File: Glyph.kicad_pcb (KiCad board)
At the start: 2 copper layers, 98 x 40.5 mm, 32 parts, among them J0 Battery Pads, J1 Shard, J2 USB-Micro, SW0 RESET, SW1 UP, SW2 DOWN, SW3 LEFT, SW4 RIGHT, SW5 BTN_A, SW6 BTN_B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

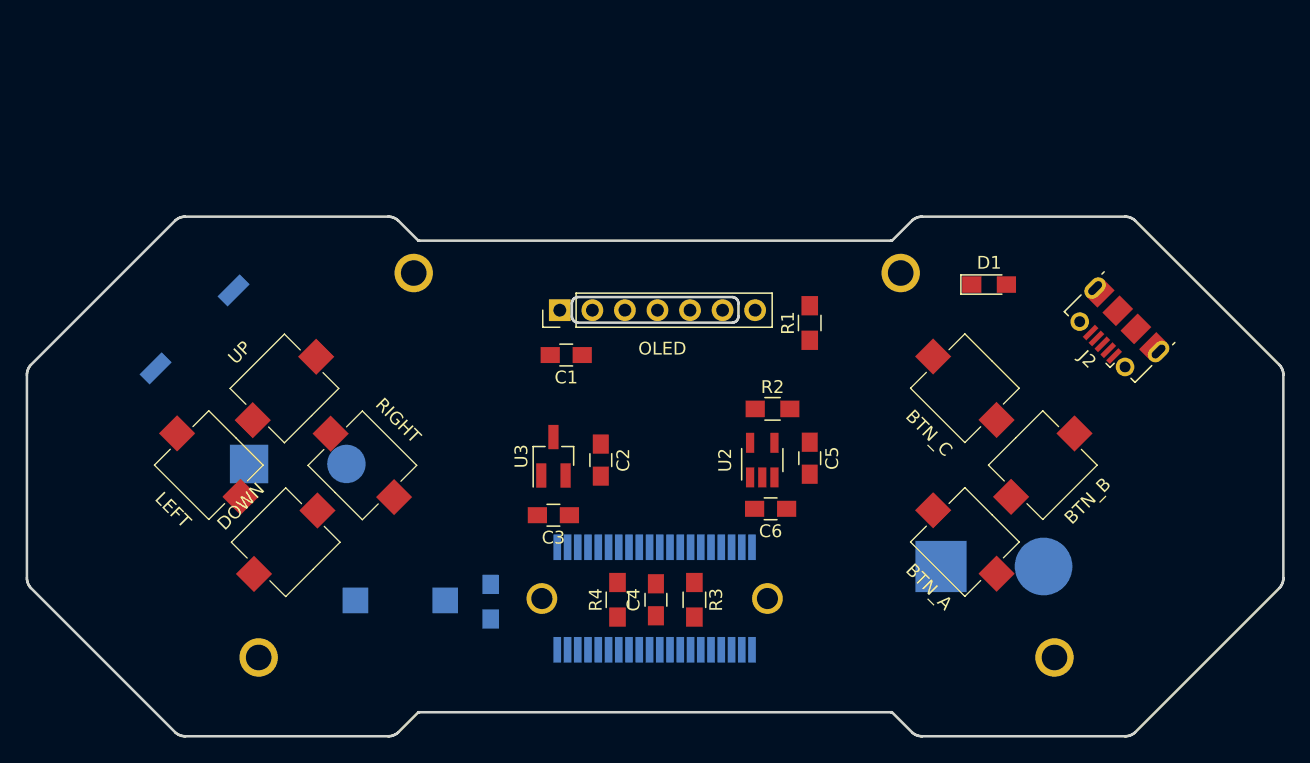
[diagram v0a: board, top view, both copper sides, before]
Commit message: initial oled components
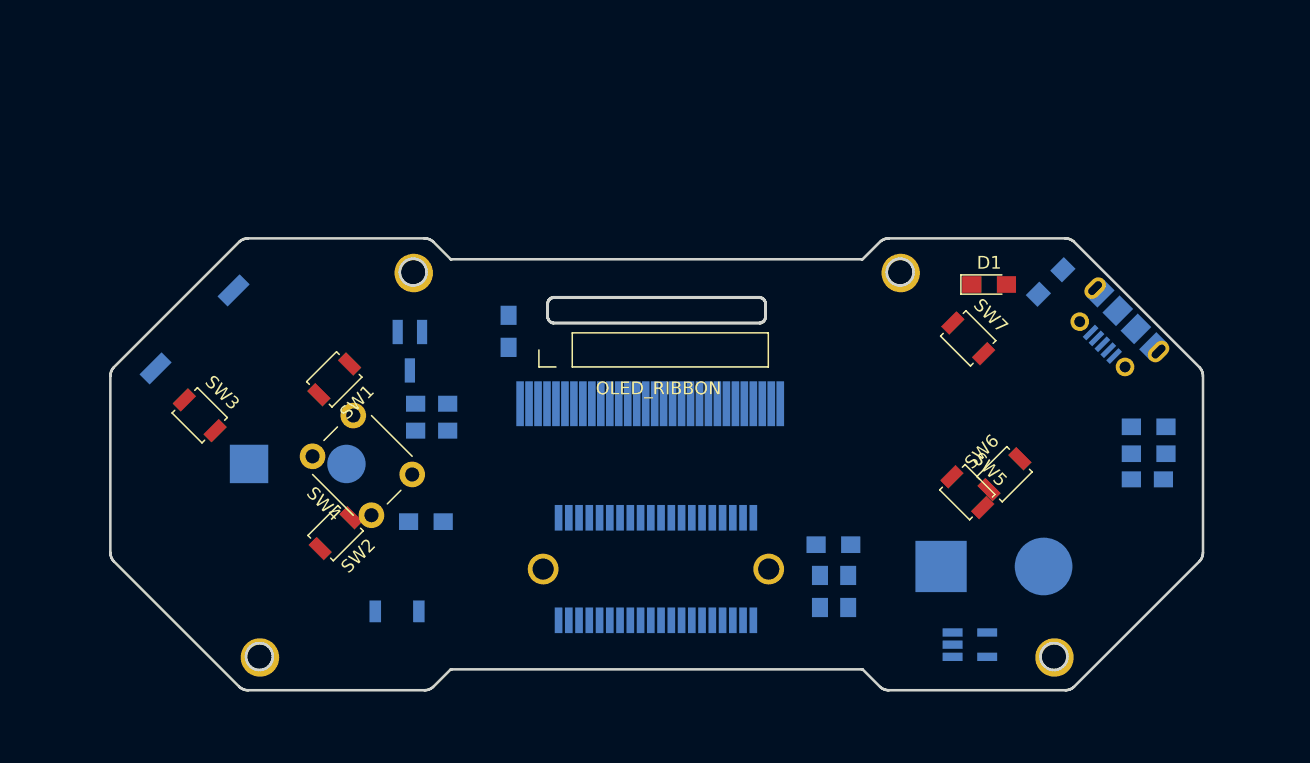
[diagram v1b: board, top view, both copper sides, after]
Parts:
- removed U1: OLED, Custom Footprints:128x64-OLED
- removed X1, X2, X3, X4: hole, Custom Footprints:M2_SCREW_HOLE
- added J3: Screw Point 1, Custom Footprints:M2_SCREW_HOLE, F.Cu at (187.1, 118.1)
- added J4: Screw Point 2, Custom Footprints:M2_SCREW_HOLE, F.Cu at (125.1, 118.1)
- added J5: Screw Point 3, Custom Footprints:M2_SCREW_HOLE, F.Cu at (137.1, 88.1)
- added J6: Screw Point 4, Custom Footprints:M2_SCREW_HOLE, F.Cu at (175.1, 88.1)
- added J7: OLED_RIBBON, Custom Footprints:1.3-OLED-bare, F.Cu at (148.2, 94.1)
- C1, C2, C3, C4, C5, C6, J2, R1, R2, R3, R4, U2, U3: moved to B.Cu
- SW0, SW1, SW2, SW3, SW5, SW6, SW7: footprint Custom Footprints:SW_SOFT_SMD_6mm -> Buttons_Switches_SMD:SW_SPST_B3U-1000P
- SW4: footprint Custom Footprints:SW_SOFT_SMD_6mm -> Buttons_Switches_THT:SW_PUSH_6mm
- moved R4 43.0 mm to (194.4, 102.2), turned to 0 degrees
- moved C4 39.5 mm to (194.3, 104.2), turned to 0 degrees
- moved R3 37.9 mm to (194.4, 100.1), turned to 180 degrees
- moved U2 21.7 mm to (180.5, 117.1), turned to 0 degrees
- moved R1 19.1 mm to (186.8, 88.8), turned to 45 degrees
- moved U3 13.9 mm to (136.8, 94.2), turned to 270 degrees
- moved C2 13.4 mm to (138.5, 100.4), turned to 180 degrees
- moved C3 12.9 mm to (138.5, 98.3)
- moved R2 11.6 mm to (169.8, 109.3)
- moved C5 10.8 mm to (171.0, 113.0), turned to 90 degrees
- moved R0 8.04 mm to (138.1, 107.5), turned to 180 degrees
- moved C6 7.51 mm to (168.8, 113.0), turned to 270 degrees
- moved C1 4.87 mm to (144.5, 92.7), turned to 270 degrees
- moved SW0 3.31 mm to (135.8, 114.5)
- moved J1 2.30 mm to (163.6, 111.2)
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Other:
- board size 98 x 40.5 mm -> 85.3 x 35.3 mm

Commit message: added OLED circuit
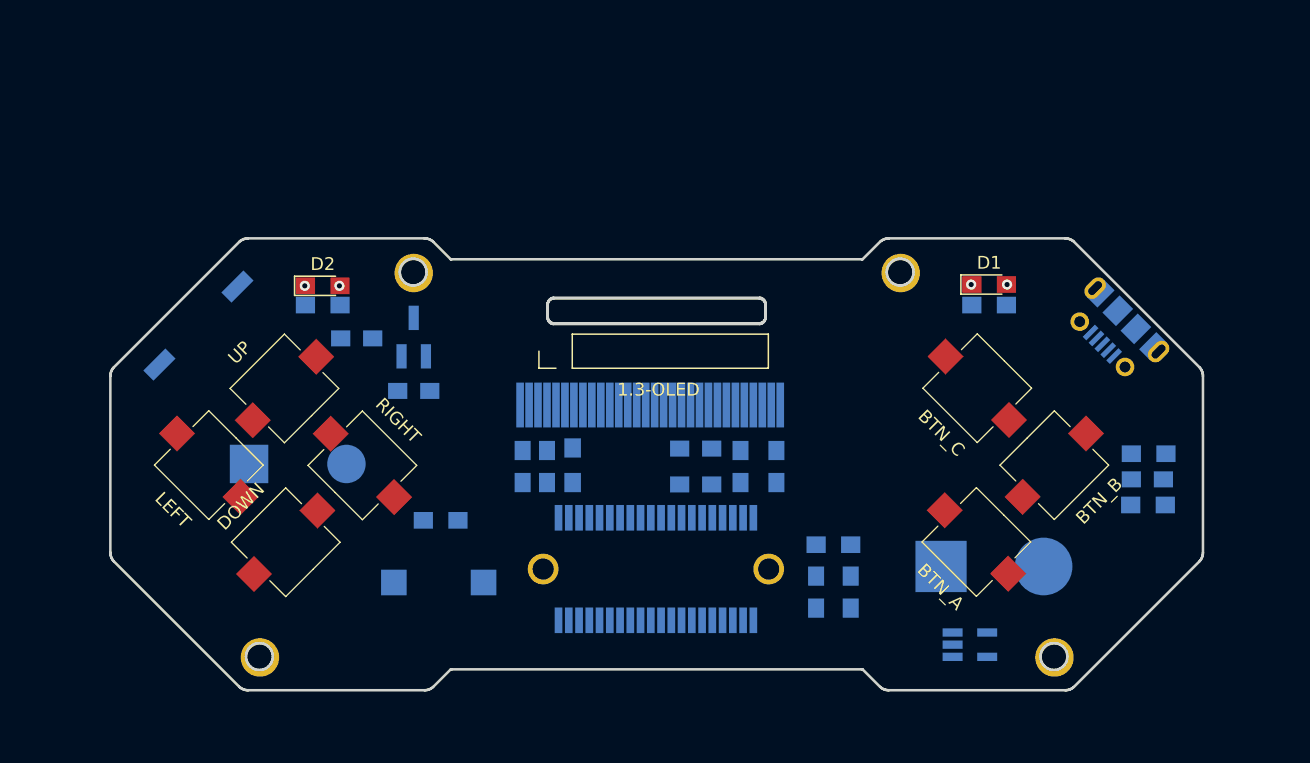
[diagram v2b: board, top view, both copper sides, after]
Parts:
- removed C1: 104, Capacitors_SMD:C_0805_HandSoldering
- removed J7: OLED_RIBBON, Custom Footprints:1.3-OLED-bare
- added C10: 1uF, Capacitors_SMD:C_0805_HandSoldering, B.Cu at (162.6, 103.2)
- added C11: 1uF, Capacitors_SMD:C_0805_HandSoldering, B.Cu at (165.4, 103.2)
- added C12: 104, Capacitors_SMD:C_0805_HandSoldering, B.Cu at (159.1, 101.8)
- added C7: 104, Capacitors_SMD:C_0805_HandSoldering, B.Cu at (159.1, 104.6)
- added C8: 47uF, Capacitors_SMD:C_0805_HandSoldering, B.Cu at (145.6, 103.2)
- added C9: 22uF, Capacitors_SMD:C_0805_HandSoldering, B.Cu at (147.5, 103.2)
- added D2: USR, LEDs:LED_0805_HandSoldering, F.Cu at (130.0, 89.1)
- added R5: 390k, Resistors_SMD:R_0805_HandSoldering, B.Cu at (149.5, 103.1)
- added R6: LED, Resistors_SMD:R_0805_HandSoldering, B.Cu at (130.0, 90.6)
- added U1: 1.3-OLED, Custom Footprints:1.3-OLED-bare, F.Cu at (148.2, 94.2)
- SW0, SW1, SW2, SW3, SW5, SW6, SW7: footprint Buttons_Switches_SMD:SW_SPST_B3U-1000P -> Custom Footprints:SW_SOFT_SMD_6mm
- SW4: footprint Buttons_Switches_THT:SW_PUSH_6mm -> Custom Footprints:SW_SOFT_SMD_6mm
- moved C2 9.28 mm to (132.7, 93.2)
- moved R3 6.10 mm to (194.4, 106.2)
- moved R1 5.13 mm to (182.0, 90.6), turned to 0 degrees
- moved C5 2.50 mm to (168.5, 113.0)
- moved C6 2.40 mm to (171.2, 113.0)
- moved C3 1.72 mm to (137.1, 97.3), turned to 0 degrees
- moved R0 1.15 mm to (139.2, 107.4)
- moved U3 1.14 mm to (137.1, 93.1), turned to 90 degrees
- moved SW8 0.42 mm to (120.3, 92.2), turned to 225 degrees
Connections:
- J1 pad 18: (no net) -> USR_LED
- J1 pad 22: D_DC -> D_RST
- J1 pad 24: D_RST -> D_DC
- J1 pad 26: D_MOSI -> D_SCK
- J1 pad 28: D_SCK -> D_MOSI
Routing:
- net USR_LED: vias 0 -> 1
- net Net-(D2-Pad1): vias 0 -> 1
- net Net-(D1-Pad1): vias 0 -> 1
- net CHARGE: vias 0 -> 1

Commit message: update layout
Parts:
- moved C8 4.24 mm to (147.0, 99.2)
- moved C9 4.18 mm to (148.7, 99.2)
- moved U3 4.12 mm to (138.1, 97.1), turned to 45 degrees
- moved R5 4.10 mm to (150.4, 99.1)
- moved C11 4.03 mm to (164.9, 99.2)
- moved C7 4.00 mm to (159.3, 100.6)
- moved C10 4.00 mm to (162.5, 99.2)
- moved C3 3.91 mm to (140.4, 99.4), turned to 45 degrees
- moved C2 3.53 mm to (135.8, 94.8), turned to 45 degrees
- moved C12 3.31 mm to (159.3, 98.5)
- moved R1 1.60 mm to (182.1, 89.0)
- moved R6 1.50 mm to (130.1, 89.1)
- moved C5 1.22 mm to (169.2, 112.0)
- moved R4 1.10 mm to (194.5, 103.3)
- moved C6 1.02 mm to (171.0, 112.0)
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
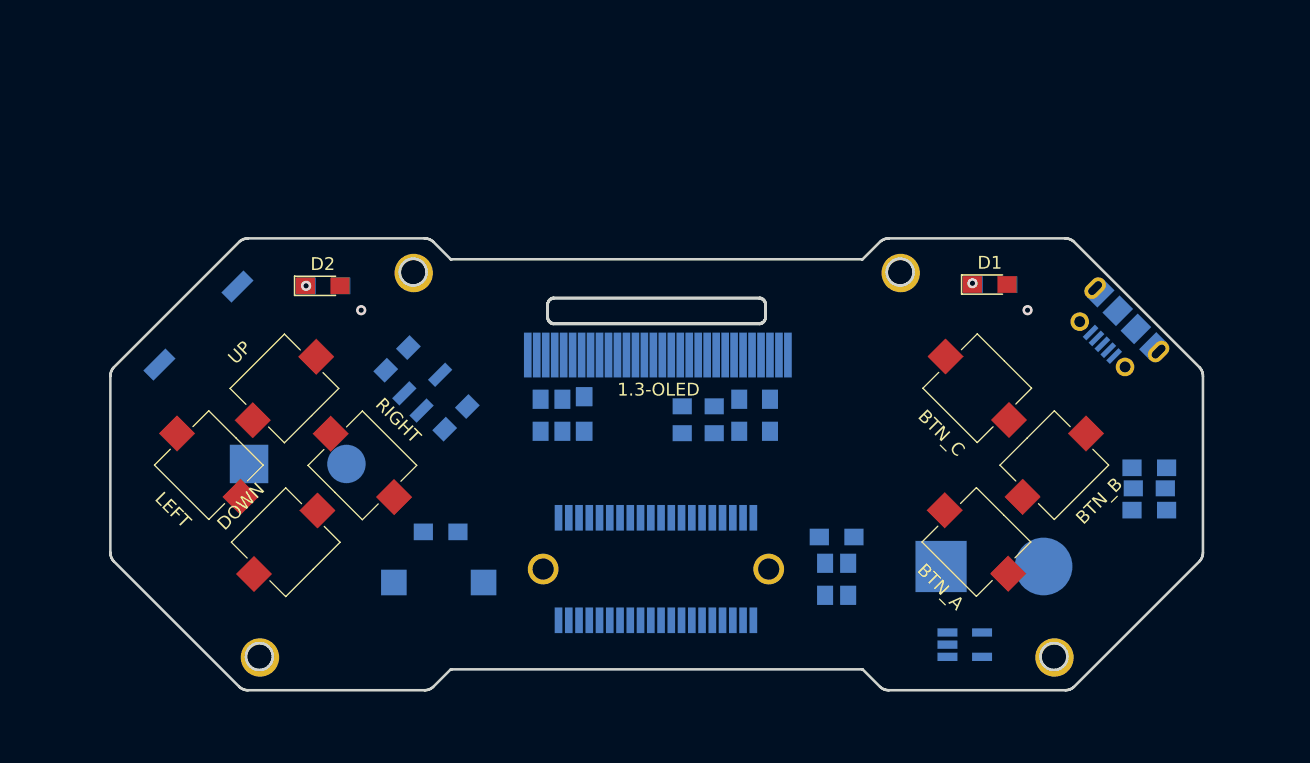
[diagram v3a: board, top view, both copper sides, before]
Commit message: new layout & traces
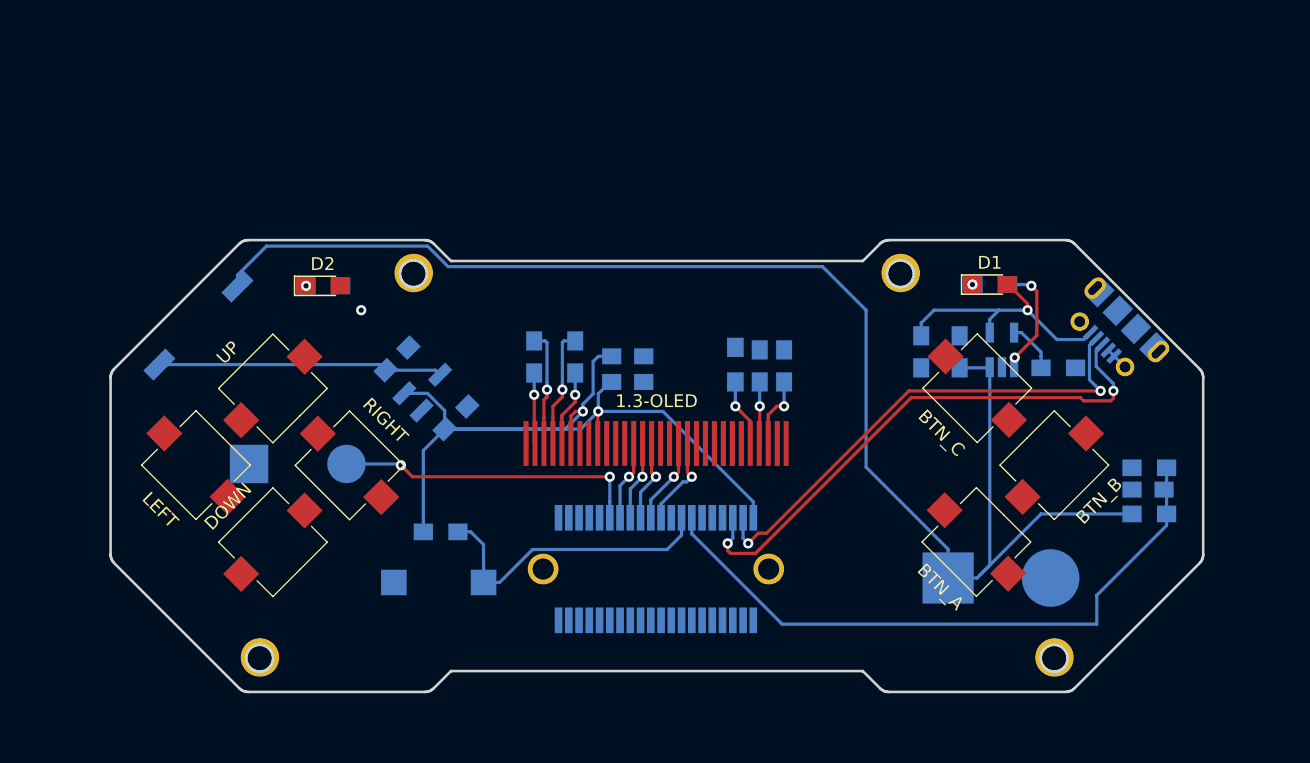
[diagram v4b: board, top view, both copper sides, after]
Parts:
- U1: footprint Custom Footprints:1.3-OLED-bare -> Custom Footprints:1.3-OLED-bare-noslot
- moved U2 23.2 mm to (183.0, 94.1), turned to 90 degrees
- moved R2 21.8 mm to (187.4, 95.5)
- moved C6 19.8 mm to (179.7, 94.2), turned to 90 degrees
- moved C8 19.4 mm to (166.0, 95.3), turned to 90 degrees
- moved C5 19.3 mm to (176.7, 94.2), turned to 270 degrees
- moved C11 19.0 mm to (146.5, 94.7), turned to 90 degrees
- moved C9 15.9 mm to (164.1, 95.3), turned to 90 degrees
- moved C10 13.6 mm to (149.7, 94.7), turned to 270 degrees
- moved R5 12.4 mm to (162.2, 95.2), turned to 90 degrees
- moved C7 6.80 mm to (153.8, 96.6), turned to 0 degrees
- moved C12 6.74 mm to (153.8, 94.6), turned to 0 degrees
- moved J0 1.05 mm to (182.8, 111.9)
- moved SW2 1.00 mm to (130.0, 108.4)
- moved SW3 1.00 mm to (119.4, 99.2)
- moved SW4 1.00 mm to (132.8, 107.0)
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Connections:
- J1 pad 20: D_CS -> D_MOSI
- J1 pad 22: D_RST -> D_SCK
- J1 pad 26: D_SCK -> D_RST
- J1 pad 28: D_MOSI -> D_CS
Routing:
- net +BATT: track 0.00 -> 111.8 mm
- net +3V3: track 0.00 -> 68.4 mm, vias 0 -> 2
- net BAT_MON: track 0.00 -> 50.2 mm
- net D+: track 0.00 -> 43.1 mm, vias 0 -> 2
- net D-: track 0.00 -> 39.3 mm, vias 0 -> 2
- net SND: track 0.00 -> 24.2 mm, vias 0 -> 2
- net RESET: track 0.00 -> 23.7 mm
- net Net-(C2-Pad1): track 0.00 -> 22.2 mm
- net CHARGE: track 0.00 -> 20.6 mm
- net Net-(C10-Pad1): track 0.00 -> 9.23 mm, vias 0 -> 1
- net Net-(C11-Pad2): track 0.00 -> 9.02 mm, vias 0 -> 1
- net Net-(R1-Pad1): track 0.00 -> 8.38 mm, vias 0 -> 2
- net D_MOSI: track 0.00 -> 7.10 mm, vias 0 -> 1
- net D_SCK: track 0.00 -> 6.70 mm, vias 0 -> 1
- net D_DC: track 0.00 -> 6.44 mm, vias 0 -> 1
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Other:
- outline, holes or cut-outs redrawn

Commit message: tracks laid out
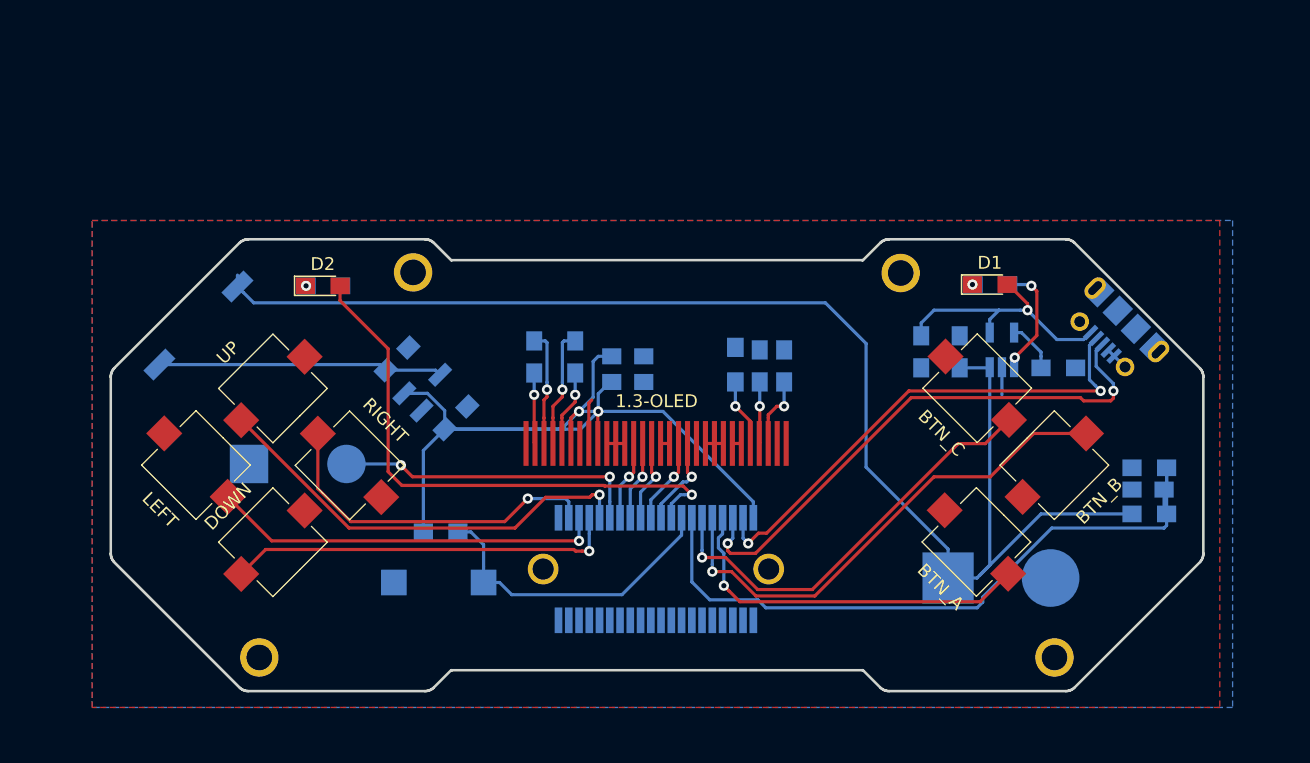
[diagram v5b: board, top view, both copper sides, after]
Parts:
- R5: value 390k -> 290k
- moved J3 58.4 mm to (137.1, 88.0)
- moved J6 58.4 mm to (125.0, 118.1)
- moved J4 58.3 mm to (175.1, 88.1)
- moved J5 58.3 mm to (187.1, 118.1)
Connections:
- J1 pad : (no net) -> GND
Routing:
- net USR_LED: track 0.00 -> 43.5 mm
- net BTN_B: track 0.00 -> 39.4 mm, vias 0 -> 1
- net UP: track 0.00 -> 34.3 mm, vias 0 -> 1
- net BTN_C: track 0.00 -> 33.6 mm, vias 0 -> 1
- net LEFT: track 0.00 -> 30.6 mm, vias 0 -> 1
- net DOWN: track 0.00 -> 30.6 mm, vias 0 -> 1
- net BTN_A: track 0.00 -> 29.2 mm, vias 0 -> 1
- net RIGHT: track 0.00 -> 27.0 mm, vias 0 -> 1
- net GND: track 1.85 -> 14.8 mm
- net BAT_MON: track 50.2 -> 54.0 mm
- net +BATT: track 111.8 -> 108.0 mm
- net +3V3: track 68.4 -> 69.8 mm
- net RESET: track 23.7 -> 24.5 mm
- added copper zone on B.Cu, net GND
- added copper zone on F.Cu, net GND
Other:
- outline, holes or cut-outs redrawn
